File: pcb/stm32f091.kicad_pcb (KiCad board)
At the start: 2 copper layers, 63.5 x 50.8 mm, 49 parts, among them J1 USB_B_Micro, J10 Touch, J2 Audio, J3 PRG, J6 UART, J7 Micro_SD_Card, J8 LCD, J9 Keypad, SW1 SW_Push, U1 LD1117S33TR_SOT223, U2 STM32F091RCTx, X1 32.768kHz(12.5pF), X2 8MHz(20pF)

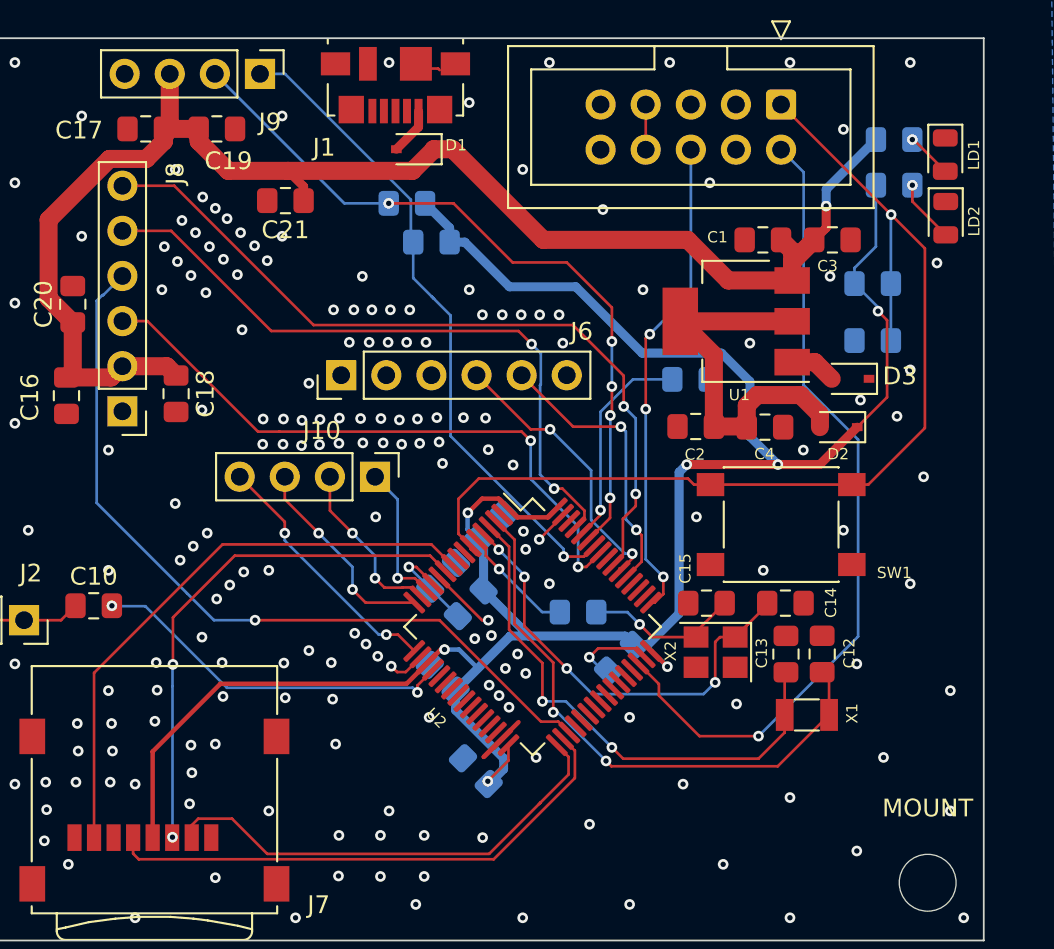
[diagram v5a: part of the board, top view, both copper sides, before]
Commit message: moved vias from under pads, fixed trace widths
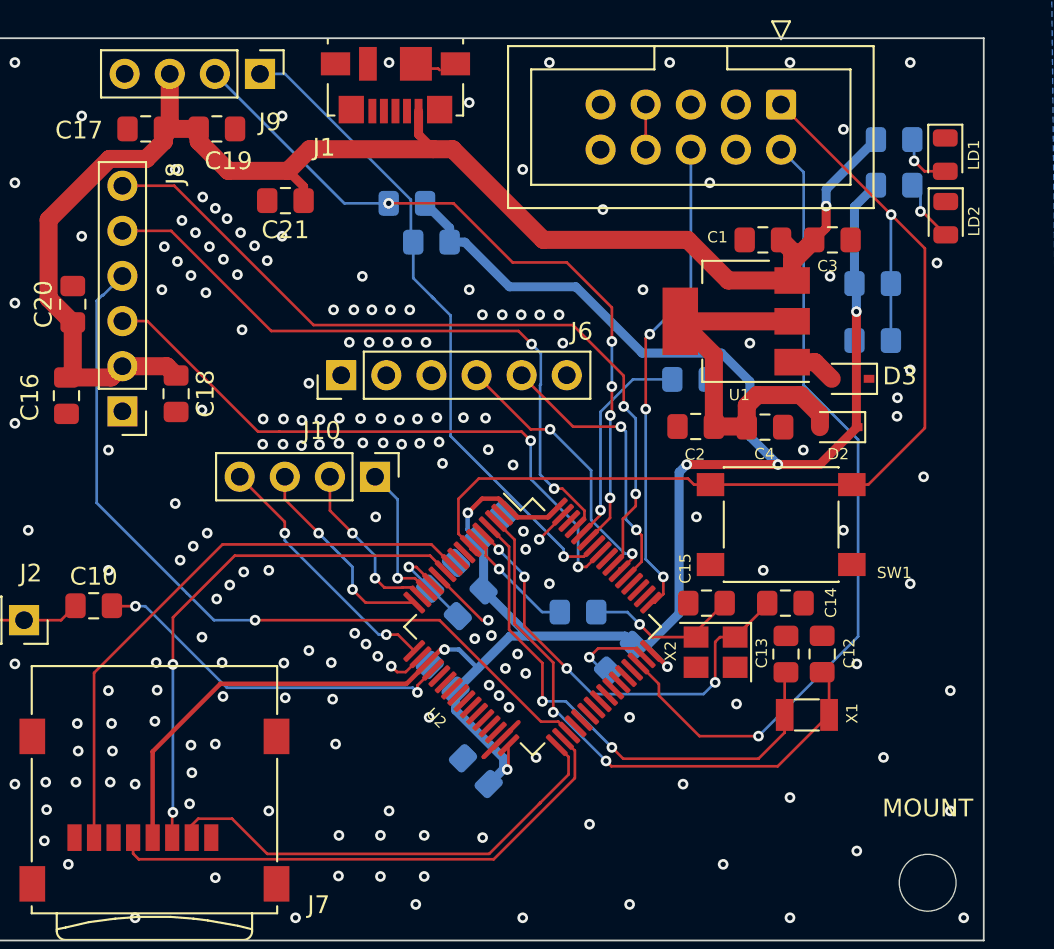
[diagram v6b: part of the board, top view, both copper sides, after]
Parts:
- removed D1: BAT60JFILM, Diode_SMD:D_SOD-323
- J3: value PRG -> Conn_02x05_Odd_Even
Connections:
- J1 pad 1: Net-(D1-Pad2) -> +5V
- J1 pad 2: (no net) -> Net-(J1-Pad2)
- J1 pad 3: (no net) -> Net-(J1-Pad3)
- J1 pad 4: (no net) -> Net-(J1-Pad4)
- J3 pad 10: (no net) -> Net-(J3-Pad10)
- J3 pad 5: (no net) -> Net-(J3-Pad5)
- J3 pad 9: (no net) -> Net-(J3-Pad9)
- J6 pad 3: (no net) -> Net-(J6-Pad3)
- J6 pad 6: (no net) -> Net-(J6-Pad6)
- J7 pad 1: (no net) -> Net-(J7-Pad1)
- J7 pad 8: (no net) -> Net-(J7-Pad8)
- U2 pad 2: (no net) -> Net-(U2-Pad2)
- U2 pad 21: (no net) -> Net-(U2-Pad21)
- U2 pad 22: (no net) -> Net-(U2-Pad22)
- U2 pad 23: (no net) -> Net-(U2-Pad23)
- U2 pad 24: (no net) -> Net-(U2-Pad24)
- U2 pad 25: (no net) -> Net-(U2-Pad25)
- U2 pad 26: (no net) -> Net-(U2-Pad26)
- U2 pad 27: (no net) -> Net-(U2-Pad27)
- U2 pad 28: (no net) -> Net-(U2-Pad28)
- U2 pad 29: (no net) -> Net-(U2-Pad29)
- U2 pad 30: (no net) -> Net-(U2-Pad30)
- U2 pad 36: (no net) -> Net-(U2-Pad36)
- U2 pad 37: (no net) -> Net-(U2-Pad37)
- U2 pad 38: (no net) -> Net-(U2-Pad38)
- U2 pad 39: (no net) -> Net-(U2-Pad39)
- U2 pad 40: (no net) -> Net-(U2-Pad40)
- U2 pad 41: (no net) -> Net-(U2-Pad41)
- U2 pad 42: (no net) -> Net-(U2-Pad42)
- U2 pad 43: (no net) -> Net-(U2-Pad43)
- U2 pad 44: (no net) -> Net-(U2-Pad44)
- U2 pad 45: (no net) -> Net-(U2-Pad45)
- U2 pad 50: (no net) -> Net-(U2-Pad50)
- U2 pad 51: (no net) -> Net-(U2-Pad51)
- U2 pad 52: (no net) -> Net-(U2-Pad52)
- U2 pad 56: (no net) -> Net-(U2-Pad56)
- U2 pad 62: (no net) -> Net-(U2-Pad62)
- U2 pad 8: (no net) -> Net-(U2-Pad8)
- U2 pad 9: (no net) -> Net-(U2-Pad9)
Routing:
- net Net-(D1-Pad2): track 2.66 -> 0.00 mm
- net +5V: track 84.6 -> 87.0 mm
- net +3V0: track 130.2 -> 127.9 mm
- net Net-(LD1-Pad2): track 2.59 -> 3.24 mm

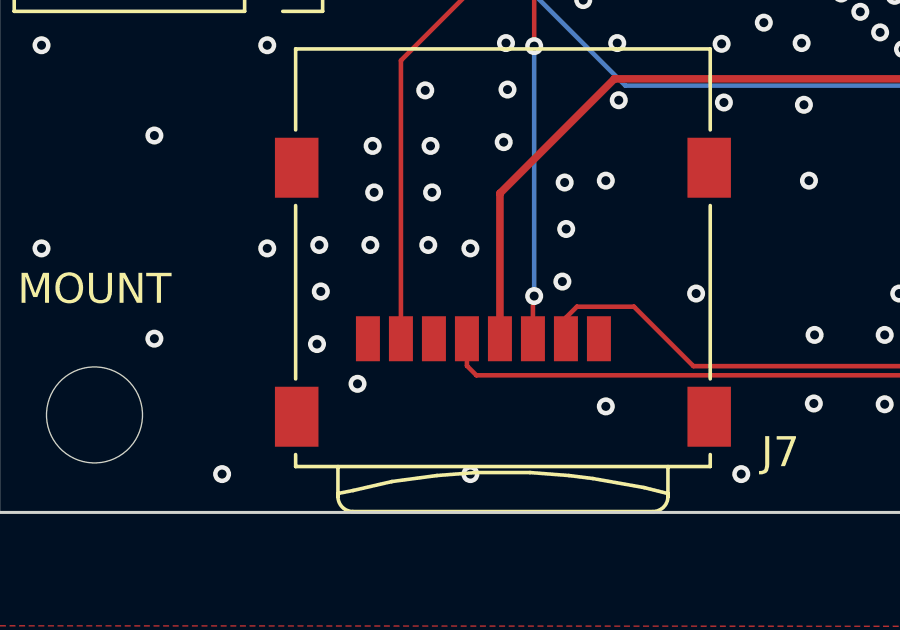
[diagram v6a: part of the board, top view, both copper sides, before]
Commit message: added SD_SPI_MISO 10K pullup
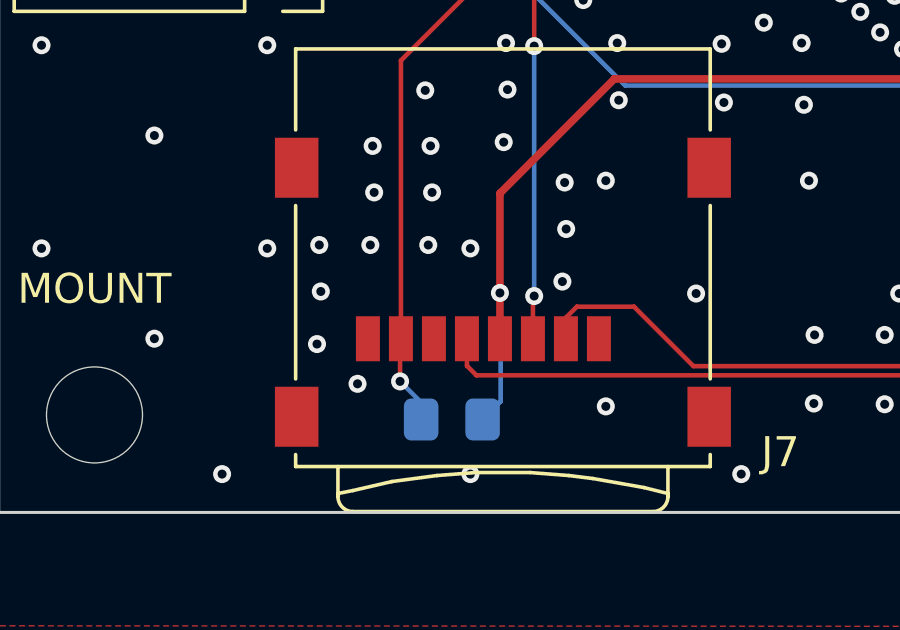
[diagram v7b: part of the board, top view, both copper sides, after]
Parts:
- added R6: 10K, Resistor_SMD:R_0805_2012Metric_Pad1.15x1.40mm_HandSolder, B.Cu at (76.1, 122.6)
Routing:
- net +3V0: track 127.9 -> 132.4 mm, vias 7 -> 8
- net /SD_SPI_MISO: track 32.9 -> 35.9 mm, vias 0 -> 1
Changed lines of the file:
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@@
     (thickness 1.6)
     (drawings 6)
-    (tracks 650)
+    (tracks 660)
     (zones 0)
-    (modules 48)
+    (modules 49)
     (nets 75)
   )
@@
   )
   (setup
-    (last_trace_width 1.016)
+    (last_trace_width 0.1524)
     (user_trace_width 0.254)
     (user_trace_width 0.508)
@@
       (net 7 /PA0))
     (model ${KISYS3DMOD}/Connector_PinHeader_2.54mm.3dshapes/PinHeader_1x04_P2.54mm_Vertical.wrl
+      (at (xyz 0 0 0))
+      (scale (xyz 1 1 1))
+      (rotate (xyz 0 0 0))
+    )
+  )
+  (module Resistor_SMD:R_0805_2012Metric_Pad1.15x1.40mm_HandSolder (layer B.Cu)
+    (at 76.06522 122.63216)
+    (descr "Resistor SMD 0805 (2012 Metric), square (rectangular) end terminal, IPC_7351 nominal with elongated pad for handsoldering. (Body size source: https://docs.google.com/spreadsheets/d/1BsfQQcO9C6DZCsRaXUlFlo91Tg2WpOkGARC1WS5S8t0/edit?usp=sharing), generated with kicad-footprint-generator")
+    (tags "resistor handsolder")
+    (attr smd)
+    (fp_text reference R6 (at 0 1.65) (layer B.SilkS)
+      (effects (font (size 1 1) (thickness 0.15)) (justify mirror))
+    )
+    (fp_text value 10K (at 0 -1.65) (layer B.Fab)
+      (effects (font (size 1 1) (thickness 0.15)) (justify mirror))
+    )
+    (fp_line (start 1.85 -0.95) (end -1.85 -0.95) (layer B.CrtYd) (width 0.05))
+    (fp_line (start 1.85 0.95) (end 1.85 -0.95) (layer B.CrtYd) (width 0.05))
+    (fp_line (start -1.85 0.95) (end 1.85 0.95) (layer B.CrtYd) (width 0.05))
+    (fp_line (start -1.85 -0.95) (end -1.85 0.95) (layer B.CrtYd) (width 0.05))
+    (fp_line (start -0.261252 -0.71) (end 0.261252 -0.71) (layer B.SilkS) (width 0.12))
+    (fp_line (start -0.261252 0.71) (end 0.261252 0.71) (layer B.SilkS) (width 0.12))
+    (fp_line (start 1 -0.6) (end -1 -0.6) (layer B.Fab) (width 0.1))
+    (fp_line (start 1 0.6) (end 1 -0.6) (layer B.Fab) (width 0.1))
+    (fp_line (start -1 0.6) (end 1 0.6) (layer B.Fab) (width 0.1))
+    (fp_line (start -1 -0.6) (end -1 0.6) (layer B.Fab) (width 0.1))
+    (fp_text user %R (at 0 0) (layer B.Fab)
+      (effects (font (size 0.5 0.5) (thickness 0.08)) (justify mirror))
+    )
+    (pad 1 smd roundrect (at -1.025 0) (size 1.15 1.4) (layers B.Cu B.Paste B.Mask) (roundrect_rratio 0.217391)
+      (net 30 /SD_SPI_MISO))
+    (pad 2 smd roundrect (at 1.025 0) (size 1.15 1.4) (layers B.Cu B.Paste B.Mask) (roundrect_rratio 0.217391)
+      (net 25 +3V0))
+    (model ${KISYS3DMOD}/Resistor_SMD.3dshapes/R_0805_2012Metric.wrl
       (at (xyz 0 0 0))
       (scale (xyz 1 1 1))
@@
   (segment (start 86.16702 84.07496) (end 86.16702 83.28016) (width 0.508) (layer F.Cu) (net 2) (status 10))
   (segment (start 85.28542 82.39856) (end 81.91842 82.39856) (width 1.016) (layer F.Cu) (net 2))
-  (segment (start 92.63762 79.03256) (end 92.63762 80.35276) (width 0.508) (layer F.Cu) (net 2))
+  (segment (start 92.63762 79.03256) (end 92.63762 80.35276) (width 0.508) (layer F.Cu) (net 2) (status 10))
   (segment (start 86.50462 81.17936) (end 85.28542 82.39856) (width 1.016) (layer F.Cu) (net 2))
   (segment (start 93.46422 81.17936) (end 86.50462 81.17936) (width 1.016) (layer F.Cu) (net 2))
@@
   (segment (start 100.417902 101.403678) (end 99.91582 101.90576) (width 0.254) (layer F.Cu) (net 25) (status 30))
   (segment (start 100.421181 101.403678) (end 100.417902 101.403678) (width 0.254) (layer F.Cu) (net 25) (status 30))
-  (segment (start 77.66702 115.092846) (end 77.66702 119.94036) (width 0.254) (layer F.Cu) (net 25) (status 20))
   (segment (start 81.481506 111.27836) (end 77.66702 115.092846) (width 0.254) (layer F.Cu) (net 25))
   (segment (start 91.960711 111.27836) (end 81.481506 111.27836) (width 0.254) (layer F.Cu) (net 25))
@@
   (segment (start 117.18014 84.41436) (end 118.38918 83.20532) (width 0.508) (layer B.Cu) (net 25) (status 20))
   (segment (start 117.18014 88.74506) (end 117.18014 84.41436) (width 0.508) (layer B.Cu) (net 25) (status 10))
+  (segment (start 77.09022 122.63216) (end 77.69082 122.03156) (width 0.1524) (layer B.Cu) (net 25))
+  (via (at 77.66702 118.41416) (size 0.6) (drill 0.3) (layers F.Cu B.Cu) (net 25))
+  (segment (start 77.69082 118.43796) (end 77.66702 118.41416) (width 0.1524) (layer B.Cu) (net 25))
+  (segment (start 77.69082 122.03156) (end 77.69082 118.43796) (width 0.1524) (layer B.Cu) (net 25))
+  (segment (start 77.66702 118.41416) (end 77.66702 119.94036) (width 0.254) (layer F.Cu) (net 25))
+  (segment (start 77.66702 115.092846) (end 77.66702 118.41416) (width 0.254) (layer F.Cu) (net 25))
   (segment (start 93.302592 105.922308) (end 93.294972 105.922308) (width 0.1524) (layer B.Cu) (net 26) (status 30))
   (segment (start 94.849452 107.469168) (end 93.302592 105.922308) (width 0.1524) (layer B.Cu) (net 26) (status 30))
@@
   (segment (start 74.36702 119.94036) (end 74.36702 110.66516) (width 0.1524) (layer F.Cu) (net 30) (status 10))
   (segment (start 81.60242 103.42976) (end 93.360941 103.42976) (width 0.1524) (layer F.Cu) (net 30))
+  (via (at 74.33802 121.36216) (size 0.6) (drill 0.3) (layers F.Cu B.Cu) (net 30))
+  (segment (start 75.04022 122.06436) (end 74.33802 121.36216) (width 0.1524) (layer B.Cu) (net 30))
+  (segment (start 75.04022 122.63216) (end 75.04022 122.06436) (width 0.1524) (layer B.Cu) (net 30))
+  (segment (start 74.33802 119.96936) (end 74.36702 119.94036) (width 0.1524) (layer F.Cu) (net 30))
+  (segment (start 74.33802 121.36216) (end 74.33802 119.96936) (width 0.1524) (layer F.Cu) (net 30))
   (segment (start 76.56702 120.84276) (end 76.56702 119.94036) (width 0.1524) (layer F.Cu) (net 31) (status 20))
   (segment (start 76.88322 121.15896) (end 76.56702 120.84276) (width 0.1524) (layer F.Cu) (net 31))
